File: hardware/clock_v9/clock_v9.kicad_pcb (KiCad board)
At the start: 2 copper layers, 119 x 92 mm, 164 parts, among them J1 RJ45, J10 KH-BNC50-3511, J11 KH-BNC50-3511, J12 Conn_01x06, J13 KH-BNC50-3511, J14 DC-063-25A, J2 Conn_01x06_Pin, J3 KH-BNC50-3511, J4 USB_C_Receptacle, J5 Conn_01x06_Pin, J6 Conn_01x04_Pin, J7 KH-BNC50-3511, J8 Conn_01x02, J9 KH-BNC50-3511, Q1 2N7002, Q10 2N7002, Q2 S8550, Q3 S8050, Q9 2N7002, SW1 LC1258OASP, U1 ADA4807-1, U10 STM32F405RGTx, U11 AMS1117-3.3, U12 BA50DD0WHFP-TR, U13 M24C02-RMN, U14 CH340C, U15 USBLC6-2P6, U16 TLV3603DCKR, U17 SN74LVC1G14DBV, U2 SN74LVC1G14DBV, U3 SN74LVC1G14DBV, U4 ADA4807-1, U5 ADA4807-1, U6 TLV3603DCKR, U7 SN74LVC1G14DBV, U8 TLV3603DCKR, U9 L78L05_SOT89, Y1 AOCJY4A-10.000MHZ-SW, Y2 16MHz

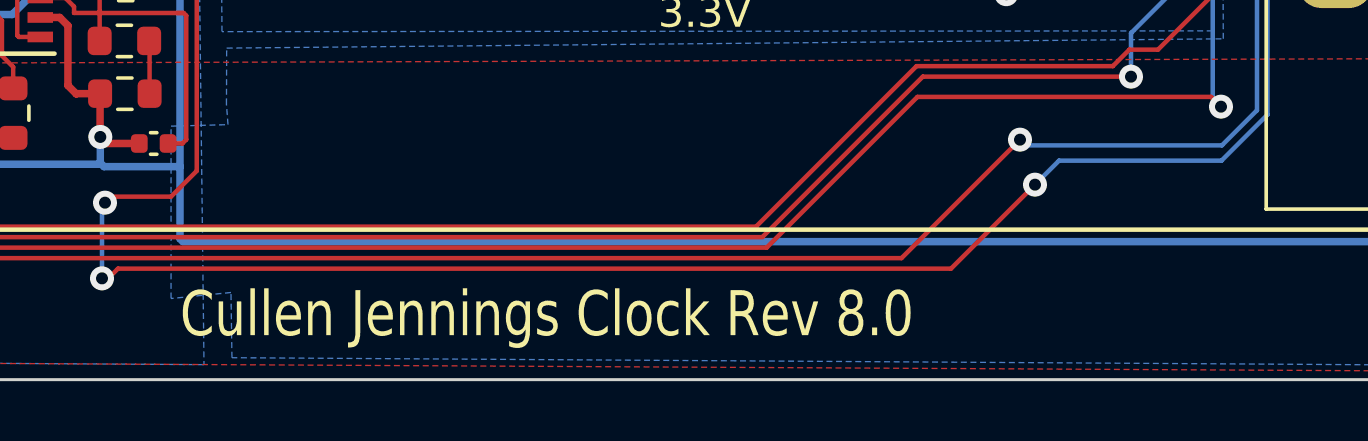
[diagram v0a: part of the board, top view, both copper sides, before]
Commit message: start USB power mon
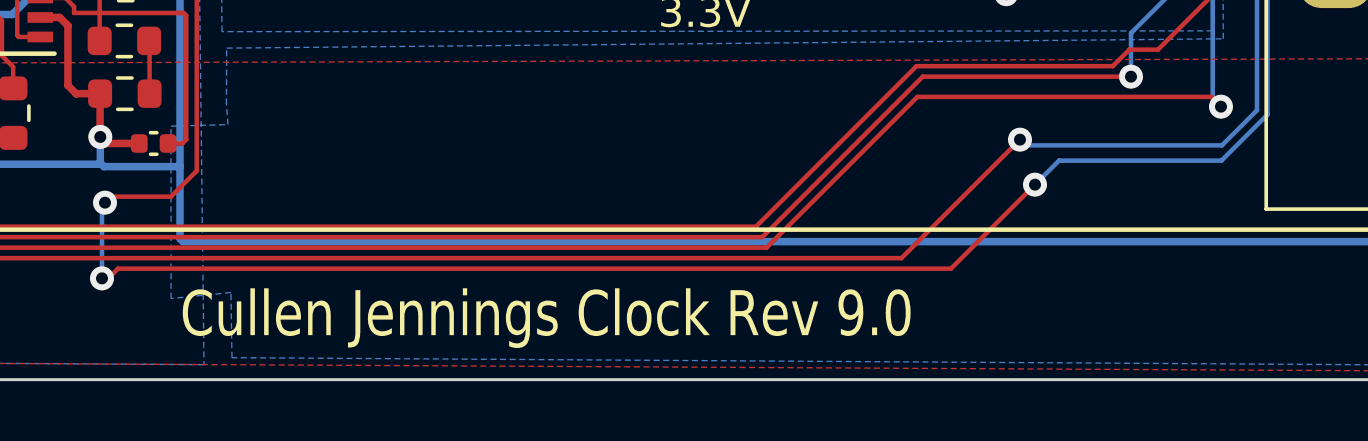
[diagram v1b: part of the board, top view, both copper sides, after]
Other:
- board text added: "Cullen Jennings Clock Rev 9.0"
- board text removed: "Cullen Jennings Clock Rev 8.0"
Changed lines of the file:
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@@
   (title_block
     (title "Clock")
-    (date "2023-11-15")
-    (rev "V8")
+    (date "2023-12-02")
+    (rev "V9.0")
     (company "Cullen Jennings")
   )
@@
   (gr_line (start 95 38) (end 95 130)
     (stroke (width 0.1) (type default)) (layer "Edge.Cuts"))
-  (gr_text "Cullen Jennings Clock Rev 8.0	\n" (at 162.4 128.7) (layer "F.SilkS")
+  (gr_text "Cullen Jennings Clock Rev 9.0	\n" (at 162.4 128.7) (layer "F.SilkS")
     (effects (font (size 1.5 1.2) (thickness 0.15)) (justify left bottom))
   )

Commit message: start routing GPS RS232 inverts
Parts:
- removed J12: Conn_01x06, Connector_JST:JST_PH_S6B-PH-SM4-TB_1x06-1MP_P2.00mm_Horizontal
- removed J6: Conn_01x04_Pin, Connector_PinHeader_2.54mm:PinHeader_1x04_P2.54mm_Vertical
- added C55: 100n, Capacitor_SMD:C_0402_1005Metric, F.Cu at (356.7, 105.0)
- added D4: 1N4148W, Diode_SMD:D_SOD-123, F.Cu at (114.2, 68.2)
- added H1: M2, MountingHole:MountingHole_2.2mm_M2, F.Cu at (57.0, 35.7)
- added H2: M2, MountingHole:MountingHole_2.2mm_M2, F.Cu at (57.0, 41.7)
- added H3: M2, MountingHole:MountingHole_2.2mm_M2, F.Cu at (57.0, 47.6)
- added H4: M2, MountingHole:MountingHole_2.2mm_M2, F.Cu at (57.0, 53.6)
- added JP3: SolderJumper_2_Bridged, Jumper:SolderJumper-2_P1.3mm_Bridged2Bar_RoundedPad1.0x1.5mm, F.Cu at (357.4, 92.5)
- added JP4: SolderJumper_2_Bridged, Jumper:SolderJumper-2_P1.3mm_Bridged2Bar_RoundedPad1.0x1.5mm, F.Cu at (153.2, 94.9)
- added JP5: SolderJumper_2_Open, Jumper:SolderJumper-2_P1.3mm_Open_RoundedPad1.0x1.5mm, F.Cu at (150.4, 108.3)
- added Q4: S8050, Package_TO_SOT_SMD:SOT-23, F.Cu at (117.8, 65.5)
- added Q5: S8050, Package_TO_SOT_SMD:SOT-23, F.Cu at (115.7, 54.7)
- added R48: 4K7, Resistor_SMD:R_0603_1608Metric, F.Cu at (118.8, 62.0)
- added R49: 1K0, Resistor_SMD:R_0603_1608Metric, F.Cu at (115.6, 57.5)
- added R50: 10K, Resistor_SMD:R_0805_2012Metric, F.Cu at (357.4, 99.3)
- added R51: 1K0, Resistor_SMD:R_0603_1608Metric, F.Cu at (340.6, 104.5)
- added R52: 1K0, Resistor_SMD:R_0603_1608Metric, F.Cu at (119.3, 69.2)
- added R53: 1K0, Resistor_SMD:R_0603_1608Metric, F.Cu at (119.3, 54.7)
- added R55: 1K0, Resistor_SMD:R_0603_1608Metric, F.Cu at (344.6, 94.5)
- added R56: 1K0, Resistor_SMD:R_0603_1608Metric, F.Cu at (344.6, 97.0)
- added R57: 1K0, Resistor_SMD:R_0603_1608Metric, F.Cu at (344.6, 99.5)
- added R65: 1K0, Resistor_SMD:R_0603_1608Metric, F.Cu at (344.6, 102.0)
- added R66: 1K0, Resistor_SMD:R_0603_1608Metric, F.Cu at (344.6, 104.5)
- added R67: 1K0, Resistor_SMD:R_0603_1608Metric, F.Cu at (344.6, 107.0)
- added R68: 1K0, Resistor_SMD:R_0603_1608Metric, F.Cu at (348.6, 92.0)
- added R69: 1K0, Resistor_SMD:R_0603_1608Metric, F.Cu at (348.6, 94.5)
- added R70: 1K0, Resistor_SMD:R_0603_1608Metric, F.Cu at (348.6, 97.0)
- added R71: 1K0, Resistor_SMD:R_0603_1608Metric, F.Cu at (348.6, 99.5)
- added U18: TMP102xxDRL, Package_TO_SOT_SMD:SOT-563, F.Cu at (357.1, 102.4)
- J2: value Conn_01x06_Pin -> Conn_01x03; footprint Connector_PinHeader_2.54mm:PinHeader_1x06_P2.54mm_Vertical -> Connector_JST:JST_PH_S3B-PH-SM4-TB_1x03-1MP_P2.00mm_Horizontal
- R33: value 2K2 -> 4K7
- moved J2 68.5 mm to (171.1, 90.2), turned to -90 degrees
- moved R33 24.9 mm to (114.0, 48.0), turned to 180 degrees
- moved R34 22.8 mm to (114.0, 49.9), turned to 180 degrees
- moved J5 20.7 mm to (176.1, 35.7), turned to 90 degrees
- moved R35 9.25 mm to (114.2, 63.8)
- moved R36 4.62 mm to (116.9, 69.2), turned to 90 degrees
- moved J8 1.10 mm to (190.3, 98.2)
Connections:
- net /AUX_PPS_MON renamed /AUX_MON_PPS
- net /PPS_MON renamed /MON_PPS
- net SYNC_IN2 renamed AUX_SYNC_IN
- J1 pad 4: /GPS_RX1 -> /GPS_RX1H
- J1 pad 7: /GPS_RX2 -> /GPS_RX2H
- J2 pad 1: /GPS_EN -> /SWDIO
- J2 pad 2: /GPS_RX1 -> GND
- J2 pad 3: /GPS_TX1H -> /SWDCLK
- J5 pad 2: /BOOT0 -> Net-(J5-Pin_2)
- J5 pad 3: /BOOT1 -> Net-(J5-Pin_3)
- J5 pad 4: /BTN1 -> Net-(J5-Pin_4)
- J5 pad 5: /DB3 -> Net-(J5-Pin_5)
- R33 pad 1: /GPS_TX2 -> GND
- R33 pad 2: /GPS_TX2H -> /GPS_RX2H
- R34 pad 2: /GPS_TX2 -> /GPS_TX2H
- R35 pad 1: /GPS_TX1 -> Net-(D4-K)
- R36 pad 2: /GPS_TX1 -> Net-(D4-K)
- U10 pad 14: AUX_CLK -> Net-(U10-PA0)
- U10 pad 42: /NCOL1 -> /USB_RX
- U10 pad 43: /LEDMY -> /USB_TX
- U10 pad 50: CLK -> Net-(U10-PA15)
- U10 pad 58: /USB_RX -> /NCOL1
- U10 pad 59: /USB_TX -> /LEDMY
- U12 pad 1: +6V -> Net-(JP5-A)
- U12 pad 4: +5V -> Net-(JP4-A)
- U14 pad 2: /USB_TX -> Net-(U14-TXD)
- U14 pad 3: /USB_RX -> Net-(U14-RXD)
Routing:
- net /USB_RX: track 153.5 -> 95.3 mm, vias 5 -> 4
- net /USB_TX: track 136.6 -> 96.0 mm
- net /GPS_RX2: track 28.9 -> 0.00 mm, vias 1 -> 0
- net /GPS_TX2H: track 28.5 -> 8.70 mm
- net /GPS_RX1H: track 0.00 -> 14.2 mm
- net /GPS_RX2H: track 0.00 -> 12.5 mm
- net GND: track 1404.3 -> 1416.0 mm, vias 60 -> 61
- net +5V: track 144.9 -> 155.5 mm
- net /GPS_EXT_PPS: track 103.5 -> 110.8 mm
- net Net-(JP4-A): track 0.00 -> 7.26 mm
- net Net-(D4-K): track 0.00 -> 6.56 mm
- net /SWDIO: track 47.0 -> 40.7 mm
- net +3.3V: track 434.6 -> 440.8 mm
- net Net-(Q4-C): track 0.00 -> 5.66 mm
- net /SWDCLK: track 57.6 -> 52.9 mm
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
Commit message: route new TX/RX
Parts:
- moved R55 219.0 mm to (125.8, 84.1), turned to 180 degrees
- moved R51 215.9 mm to (125.8, 82.4)
- moved H3 159.5 mm to (195.4, 126.9)
- moved H2 139.8 mm to (196.8, 40.6)
- moved H4 91.7 mm to (111.6, 127.3)
- moved H1 67.9 mm to (124.7, 41.4)
- moved C1 25.4 mm to (113.8, 45.5)
- moved R1 16.3 mm to (115.4, 59.6), turned to 0 degrees
- moved C4 13.7 mm to (101.2, 69.5)
- moved U2 13.7 mm to (105.8, 68.3)
- moved R4 13.7 mm to (101.3, 67.0)
- moved C11 13.7 mm to (108.6, 68.9)
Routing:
- net /NCOL1: track 0.00 -> 36.2 mm, vias 0 -> 3
- net /LEDMY: track 38.2 -> 66.0 mm, vias 2 -> 5
- net Net-(U14-TXD): track 0.00 -> 19.5 mm, vias 0 -> 2
- net /USB_RX: track 95.3 -> 76.2 mm
- net Net-(U14-RXD): track 0.00 -> 18.0 mm, vias 0 -> 2
- net PPS_OUT: track 99.3 -> 115.6 mm
- net /USB_TX: track 96.0 -> 80.8 mm, vias 4 -> 2
- net +5V: track 155.5 -> 142.6 mm
- net +3.3V: track 440.8 -> 449.8 mm, vias 21 -> 19
- net /GPS_TX1H: track 36.6 -> 29.6 mm
- net /GPS_RX1: track 104.5 -> 99.3 mm
- net /GPS_EN: track 24.3 -> 29.0 mm, vias 0 -> 1
- net GND: track 1416.0 -> 1417.3 mm
- net /GPS_TX1: track 81.8 -> 80.6 mm
- net AUX_GPS_PPS: track 55.4 -> 56.4 mm

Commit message: new compenets all placed
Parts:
- removed R39: 200R, Resistor_SMD:R_0805_2012Metric
- added R72: 1K0, Resistor_SMD:R_0603_1608Metric, F.Cu at (170.0, 61.2)
- moved R71 238.3 mm to (110.3, 93.6)
- moved R70 236.2 mm to (112.4, 96.2), turned to -90 degrees
- moved R56 212.5 mm to (132.5, 83.2)
- moved JP3 203.9 mm to (154.7, 114.2), turned to -90 degrees
- moved R50 202.9 mm to (154.9, 110.8), turned to 90 degrees
- moved R69 198.6 mm to (150.6, 110.6)
- moved R57 192.5 mm to (153.3, 121.1), turned to 90 degrees
- moved U18 191.8 mm to (168.3, 68.9), turned to 90 degrees
- moved C55 191.6 mm to (169.0, 66.4), turned to 90 degrees
- moved R65 172.4 mm to (179.3, 52.8)
- moved R67 170.8 mm to (182.6, 52.8)
- moved R66 166.6 mm to (186.2, 52.8), turned to 180 degrees
- moved R68 163.8 mm to (189.5, 52.8), turned to 180 degrees
- moved R40 20.8 mm to (179.3, 44.5)
- moved J5 14.5 mm to (177.9, 50.1)
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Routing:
- net CLK: track 92.6 -> 9.01 mm, vias 4 -> 2
- net Net-(U10-PA15): track 0.00 -> 82.5 mm, vias 0 -> 2
- net Net-(U10-PA0): track 0.00 -> 53.9 mm, vias 0 -> 4
- net AUX_CLK: track 76.3 -> 23.4 mm, vias 6 -> 4
- net +3.3V: track 449.8 -> 468.1 mm, vias 19 -> 21
- net /BTN1: track 41.8 -> 26.1 mm, vias 3 -> 2
- net /SCL: track 15.9 -> 29.3 mm
- net /AUD_IN: track 0.00 -> 11.4 mm
- net Net-(R72-Pad1): track 73.0 -> 83.2 mm
- net /DB3: track 22.3 -> 12.8 mm
- net GND: track 1417.3 -> 1426.0 mm, vias 61 -> 65
- net /SDA: track 16.4 -> 24.9 mm
- net /BOOT1: track 38.2 -> 33.2 mm
- net /BOOT0: track 47.3 -> 43.4 mm
- net Net-(J5-Pin_5): track 0.00 -> 2.95 mm
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
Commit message: rough route
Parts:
- moved R68 0.85 mm to (190.4, 52.8)
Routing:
- net /AUD_IN: track 11.4 -> 95.6 mm, vias 0 -> 4
- net /LED1: track 0.00 -> 66.4 mm, vias 0 -> 2
- net /LED10: track 0.00 -> 58.7 mm, vias 0 -> 4
- net /LED9: track 0.00 -> 51.2 mm, vias 0 -> 4
- net /NCOL1: track 36.2 -> 0.00 mm, vias 3 -> 0
- net GND: track 1426.0 -> 1448.3 mm, vias 65 -> 67
- net /BTN1: track 26.1 -> 48.3 mm, vias 2 -> 6
- net /SCL: track 29.3 -> 47.4 mm, vias 0 -> 2
- net /SDA: track 24.9 -> 41.2 mm, vias 2 -> 4
- net /LEDMY: track 66.0 -> 50.6 mm, vias 5 -> 4
- net /BOOT0: track 43.4 -> 50.3 mm
- net /DB3: track 12.8 -> 16.9 mm
- net /BOOT1: track 33.2 -> 29.6 mm
- net +3.3V: track 468.1 -> 471.0 mm
- net +5V: track 142.6 -> 139.8 mm
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
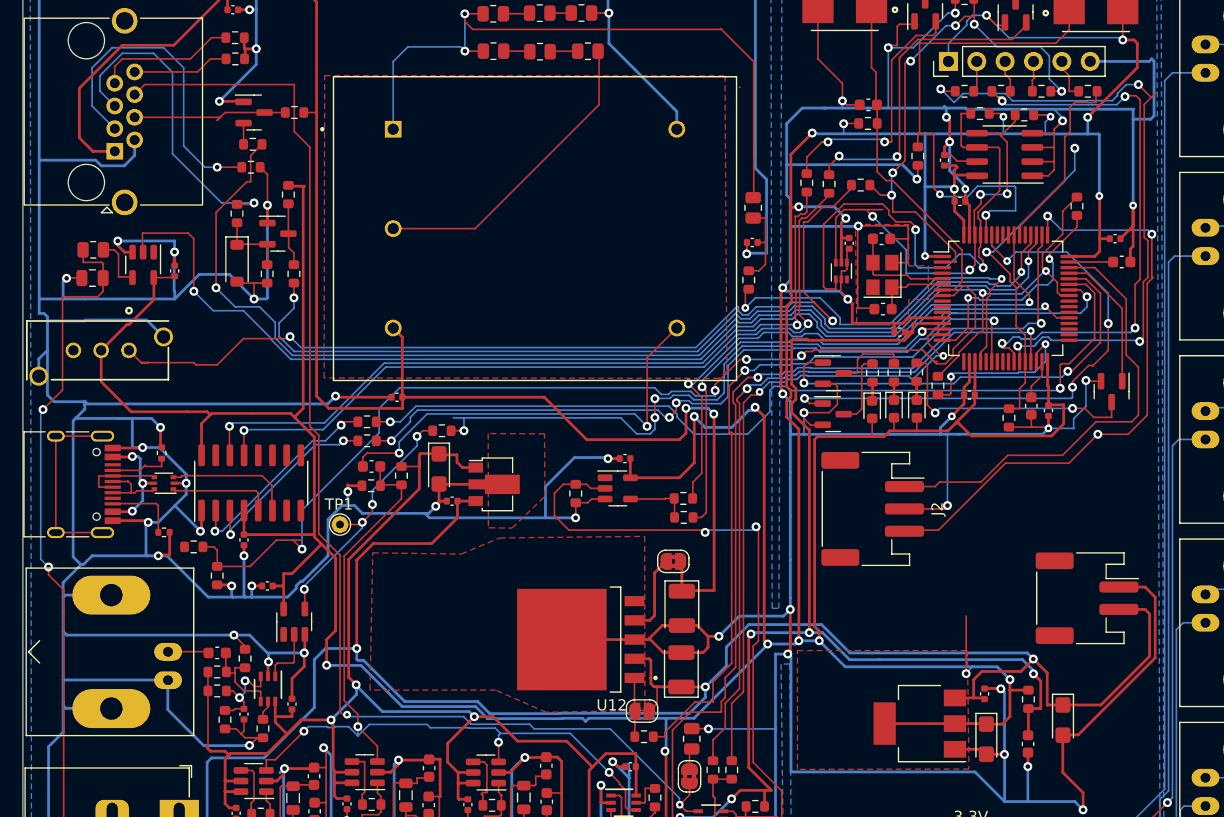
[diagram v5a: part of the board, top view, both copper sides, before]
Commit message: fix clearances
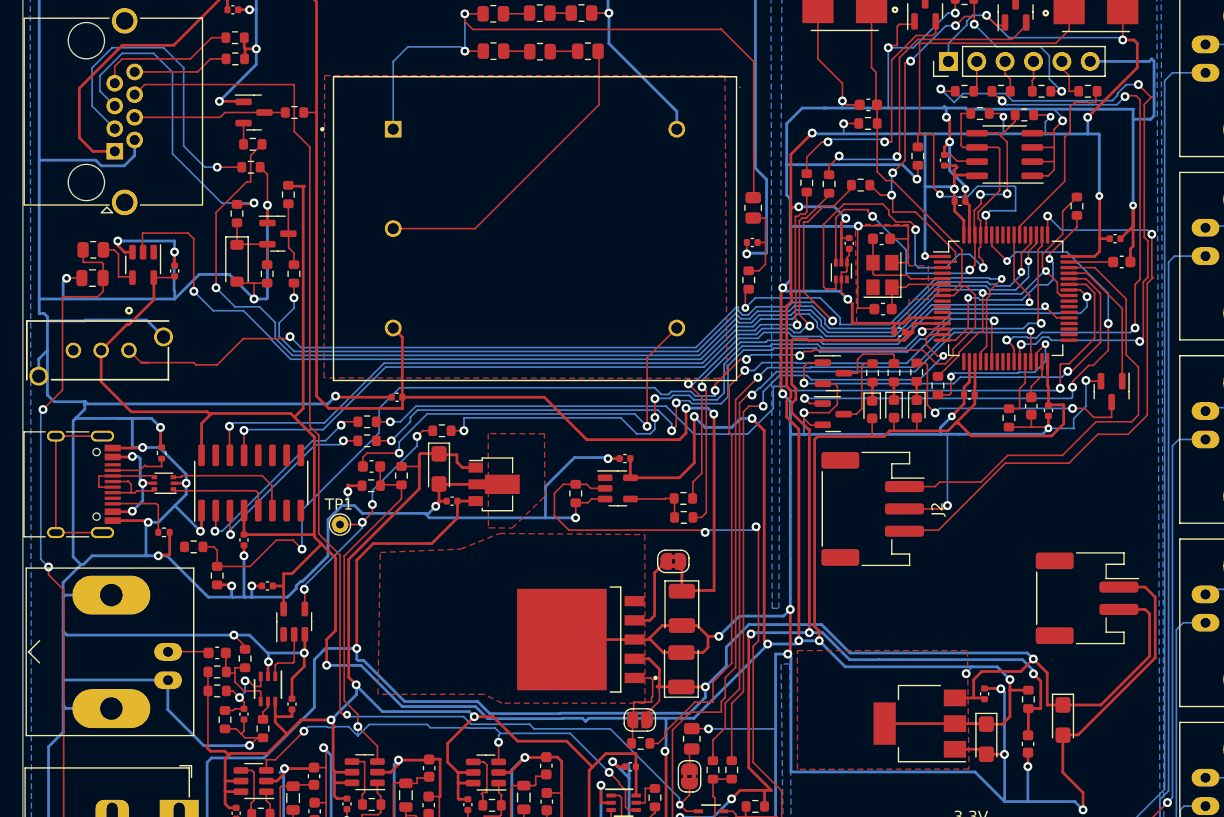
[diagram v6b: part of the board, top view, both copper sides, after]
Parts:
- moved JP5 0.82 mm to (150.2, 109.1)
- moved R69 0.67 mm to (150.3, 111.2)
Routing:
- net /BOOT1: track 29.6 -> 5.37 mm, vias 2 -> 0
- net +3.3V: track 471.0 -> 461.9 mm
- net Net-(JP5-A): track 5.27 -> 9.36 mm
- net /AUD_IN: track 95.6 -> 93.0 mm
- net /LED9: track 51.2 -> 49.1 mm
- net /SDA: track 41.2 -> 39.9 mm
- net +6V: track 162.6 -> 163.7 mm
- net /GPS_RX1H: track 14.7 -> 13.7 mm
- net Net-(U10-PA0): track 54.3 -> 53.3 mm
- net /LED10: track 58.7 -> 57.8 mm
- net Net-(U10-PA15): track 83.0 -> 82.3 mm
- net GPS_PPS: track 65.8 -> 65.2 mm
- net AUX_GPS_PPS: track 56.2 -> 56.8 mm
- net /USB_RX: track 76.4 -> 76.9 mm
- net /SWDCLK: vias 3 -> 2

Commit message: update
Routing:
- net GND: track 1448.8 -> 1444.3 mm
- net +3.3V: track 461.9 -> 464.4 mm
- net +5V: track 139.6 -> 138.2 mm
- net /OCXO_OUT: track 38.8 -> 37.5 mm
- net /LED10: track 57.8 -> 56.8 mm
- net /GPS_RX1: track 100.3 -> 99.5 mm
- net SYNC_IN: track 51.8 -> 51.2 mm
- net +5VA: track 130.3 -> 129.7 mm

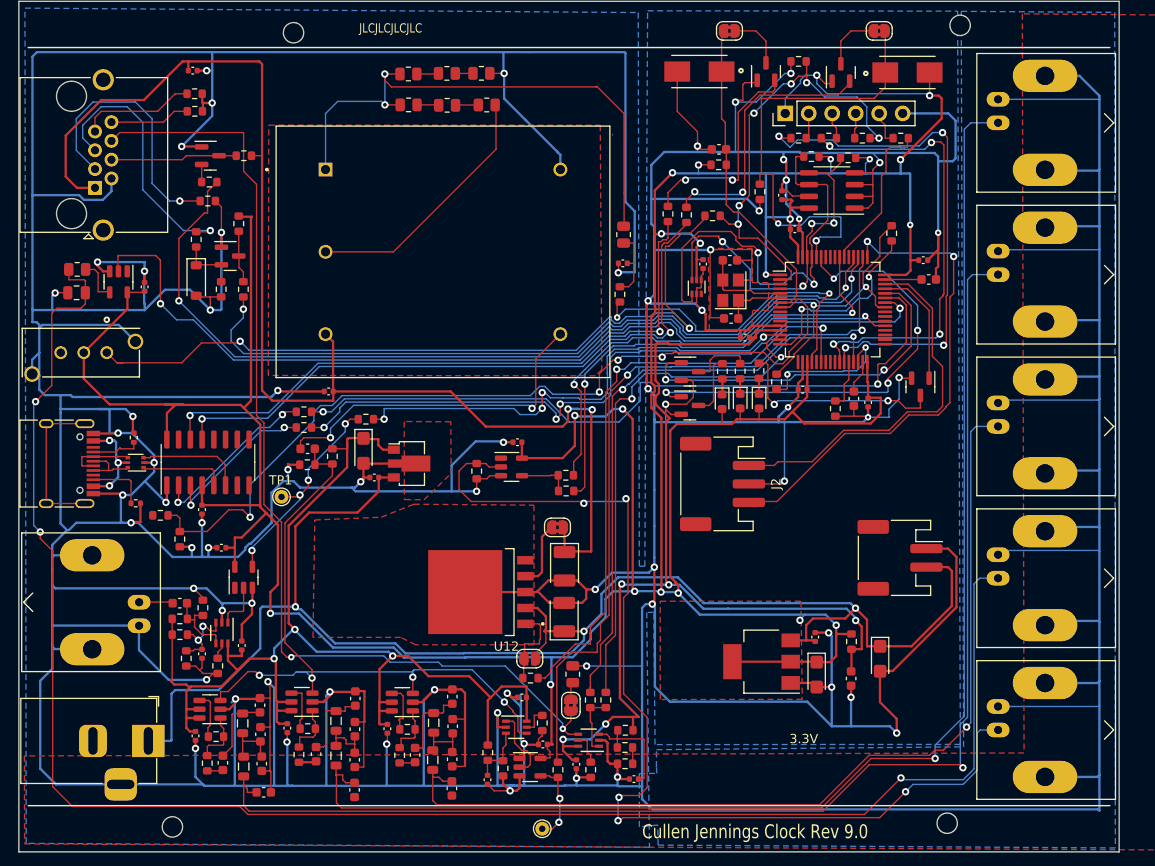
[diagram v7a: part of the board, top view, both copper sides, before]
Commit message: update PCB design rules for clock
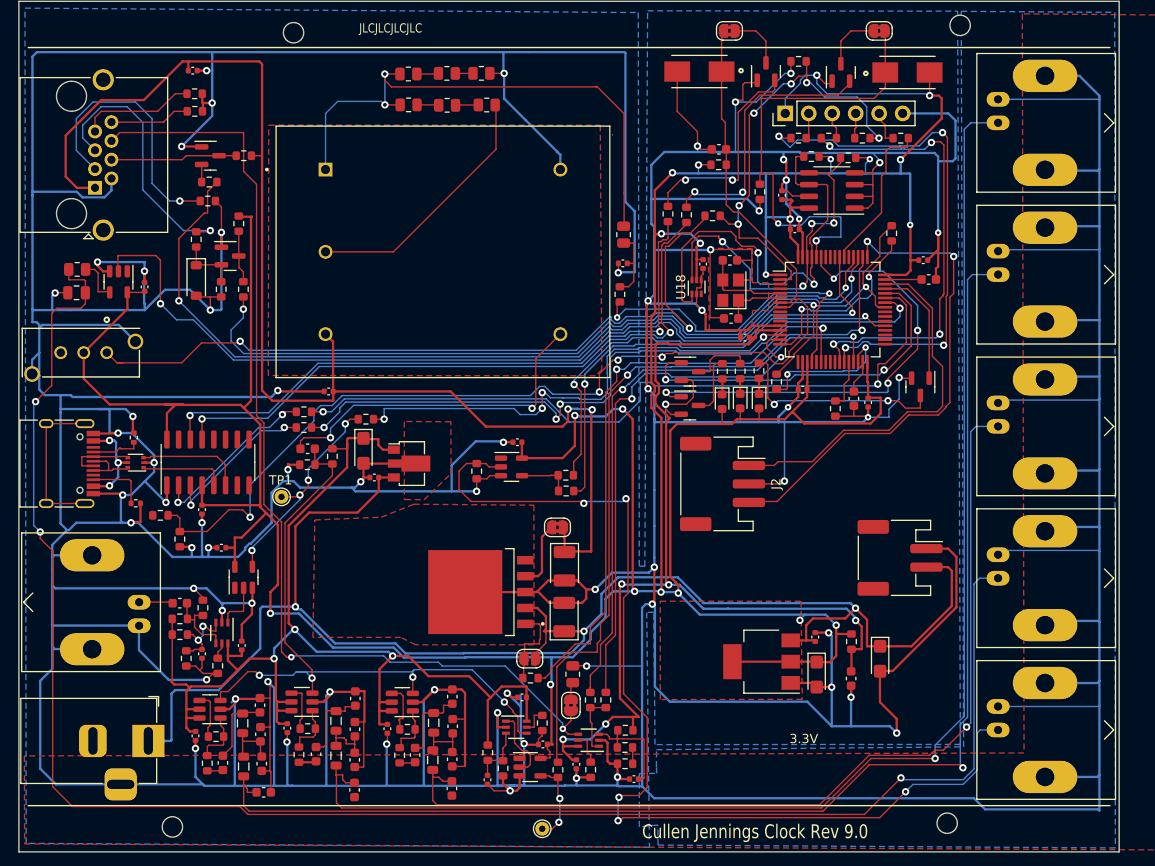
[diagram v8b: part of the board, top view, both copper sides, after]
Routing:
- net GND: track 1444.3 -> 1443.4 mm
